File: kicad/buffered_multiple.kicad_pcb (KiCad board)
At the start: 2 copper layers, 24 x 24 mm, 18 parts, among them J1 InputJack1, J2 OutputJack1, J3 OutputJack2, J4 OutputJack3, J5 power_supply, U1 TL074

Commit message: Changed format of KiCAD files from v5 to v6
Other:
- net class Default removed

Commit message: Correct footprint for power. One resistor was connected wrong way
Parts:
- J1, J2, J3, J4: footprint eurorack:PJ392-3.5mm-jack-vertical-SRT -> open-source-modular:PJ392-3.5mm-jack-vertical-SRT
- J5: footprint Connect:PINHEAD1-3 -> open-source-modular:eurorack-tile-power-connector
- moved J5 2.56 mm to (191.7, 112.5), turned to -90 degrees
- turned R7 to -90 degrees
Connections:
- net output_1 renamed Net-(J2-PadT)
- net output_2 renamed Net-(J3-PadT)
- net output_3 renamed Net-(J4-PadT)
- J1 pad R: Net-(J1-PadR) -> unconnected-(J1-PadR)
- J2 pad R: Net-(J2-PadR) -> unconnected-(J2-PadR)
- J3 pad R: Net-(J3-PadR) -> unconnected-(J3-PadR)
- J4 pad R: Net-(J4-PadR) -> unconnected-(J4-PadR)
- R7 pad 1: GND -> Net-(J1-PadT)
- R7 pad 2: Net-(J1-PadT) -> GND

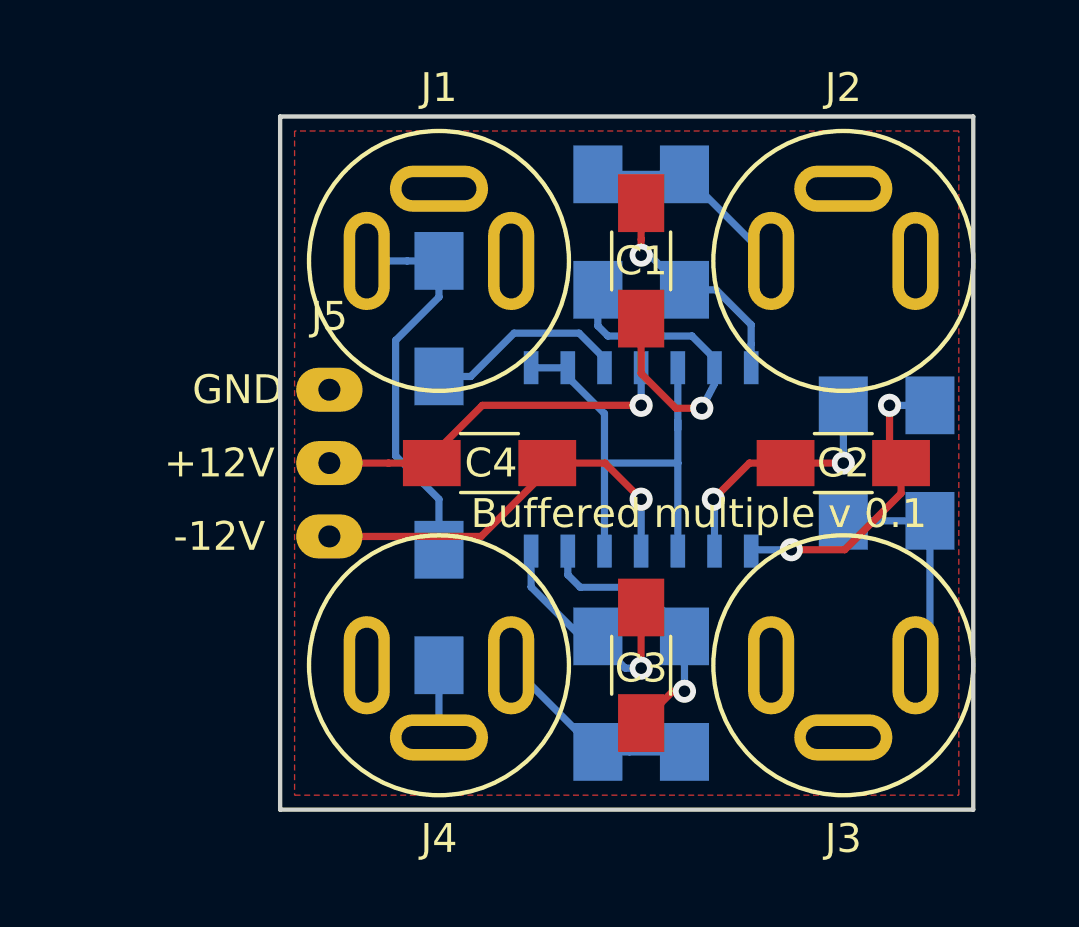
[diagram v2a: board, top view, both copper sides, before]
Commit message: Moved component references so they are visible on populated board
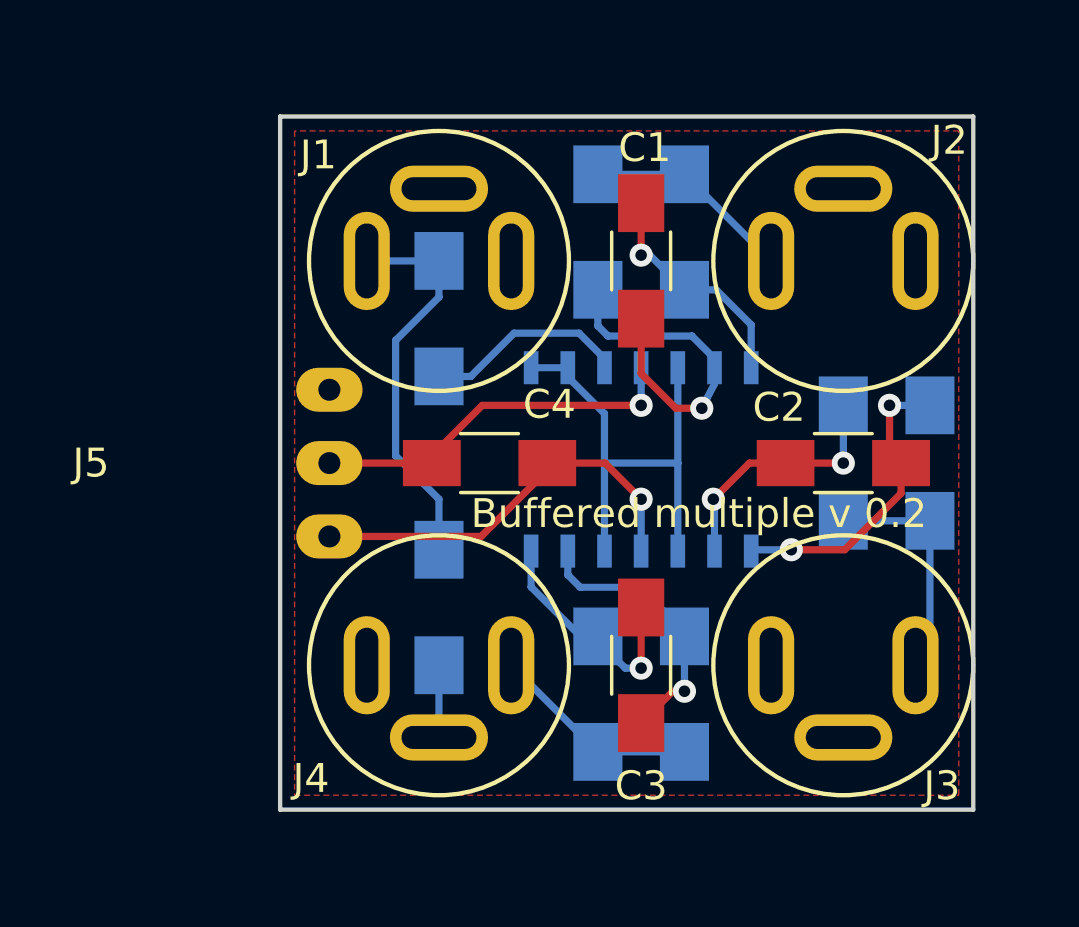
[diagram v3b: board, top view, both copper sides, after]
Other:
- board text added: "Buffered multiple v 0.2"
- board text removed: "+V"
- board text removed: "-V"
- board text removed: "Buffered multiple v 0.1"
- board text removed: "GND"

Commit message: Added gerbers for updated PCB
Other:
- rule pad_to_mask_clearance: 0.051 -> 0
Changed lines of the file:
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@@
   )
   (setup
-    (pad_to_mask_clearance 0.051)
-    (solder_mask_min_width 0.25)
+    (stackup
+      (layer "F.SilkS" (type "Top Silk Screen"))
+      (layer "F.Paste" (type "Top Solder Paste"))
+      (layer "F.Mask" (type "Top Solder Mask") (thickness 0.01))
+      (layer "F.Cu" (type "copper") (thickness 0.035))
+      (layer "dielectric 1" (type "core") (thickness 1.51) (material "FR4") (epsilon_r 4.5) (loss_tangent 0.02))
+      (layer "B.Cu" (type "copper") (thickness 0.035))
+      (layer "B.Mask" (type "Bottom Solder Mask") (thickness 0.01))
+      (layer "B.Paste" (type "Bottom Solder Paste"))
+      (layer "B.SilkS" (type "Bottom Silk Screen"))
+      (copper_finish "None")
+      (dielectric_constraints no)
+    )
+    (pad_to_mask_clearance 0)
     (grid_origin 202.5 112.5)
     (pcbplotparams
@@
       (outputformat 1)
       (mirror false)
-      (drillshape 1)
+      (drillshape 0)
       (scaleselection 1)
-      (outputdirectory "")
+      (outputdirectory "../gerbers/")
     )
   )
